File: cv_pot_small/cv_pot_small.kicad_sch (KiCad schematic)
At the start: 12 parts, among them J1 I/O connector, U1 HT7550-1, U2 LMV321IDBVR

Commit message: Updated components for JLCPCB PCBA
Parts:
- C1, C2: footprint Capacitor_SMD:C_0603_1608Metric -> Capacitor_SMD:C_0805_2012Metric; LCSC (none) -> C15850
- C3: footprint Capacitor_SMD:C_0603_1608Metric -> Capacitor_SMD:C_0402_1005Metric; LCSC (none) -> C307331
- D1: value LL4148 -> 1N4148W; footprint Diode_SMD:D_MiniMELF -> Diode_SMD:D_SOD-123; LCSC (none) -> C81598
- R1: value 5k -> 4.7k; footprint Resistor_SMD:R_0603_1608Metric -> Resistor_SMD:R_0402_1005Metric; LCSC (none) -> C25900
- U1: LCSC (none) -> C16106
- U2: LCSC (none) -> C7972
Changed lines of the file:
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@@
     (in_bom yes) (on_board yes) (fields_autoplaced)
     (property "Reference" "D1" (id 0) (at 92.71 43.5442 0))
-    (property "Value" "LL4148" (id 1) (at 92.71 46.0811 0))
-    (property "Footprint" "Diode_SMD:D_MiniMELF" (id 2) (at 92.71 48.26 90)
+    (property "Value" "1N4148W" (id 1) (at 92.71 46.0811 0))
+    (property "Footprint" "Diode_SMD:D_SOD-123" (id 2) (at 92.71 48.26 90)
       (effects (font (size 1.27 1.27)) hide)
     )
     (property "Datasheet" "~" (id 3) (at 92.71 48.26 90)
       (effects (font (size 1.27 1.27)) hide)
+    )
+    (property "LCSC" "C81598" (id 4) (at 92.71 48.26 0)
+      (effects (font (size 0 0)) hide)
     )
     (pin "1")
@@
       (effects (font (size 1.27 1.27)) (justify left))
     )
-    (property "Value" "5k" (id 1) (at 117.348 109.6522 0)
-      (effects (font (size 1.27 1.27)) (justify left))
-    )
-    (property "Footprint" "Resistor_SMD:R_0603_1608Metric" (id 2) (at 113.792 107.95 90)
+    (property "Value" "4.7k" (id 1) (at 117.348 109.6522 0)
+      (effects (font (size 1.27 1.27)) (justify left))
+    )
+    (property "Footprint" "Resistor_SMD:R_0402_1005Metric" (id 2) (at 113.792 107.95 90)
       (effects (font (size 1.27 1.27)) hide)
     )
@@
       (effects (font (size 1.27 1.27)) hide)
     )
+    (property "LCSC" "C25900" (id 4) (at 115.57 107.95 0)
+      (effects (font (size 1.524 1.524)) hide)
+    )
     (pin "1")
     (pin "2")
@@
       (effects (font (size 1.27 1.27)) (justify left))
     )
-    (property "Footprint" "Capacitor_SMD:C_0603_1608Metric" (id 2) (at 99.06 54.61 0)
+    (property "Footprint" "Capacitor_SMD:C_0805_2012Metric" (id 2) (at 99.06 54.61 0)
       (effects (font (size 1.27 1.27)) hide)
     )
     (property "Datasheet" "~" (id 3) (at 99.06 54.61 0)
       (effects (font (size 1.27 1.27)) hide)
+    )
+    (property "LCSC" "C15850" (id 4) (at 99.06 54.61 0)
+      (effects (font (size 1.524 1.524)) hide)
     )
     (pin "1")
@@
       (effects (font (size 1.27 1.27)) (justify left))
     )
-    (property "Footprint" "Capacitor_SMD:C_0603_1608Metric" (id 2) (at 120.65 54.61 0)
+    (property "Footprint" "Capacitor_SMD:C_0805_2012Metric" (id 2) (at 120.65 54.61 0)
       (effects (font (size 1.27 1.27)) hide)
     )
     (property "Datasheet" "~" (id 3) (at 120.65 54.61 0)
       (effects (font (size 1.27 1.27)) hide)
+    )
+    (property "LCSC" "C15850" (id 4) (at 120.65 54.61 0)
+      (effects (font (size 1.524 1.524)) hide)
     )
     (pin "1")
@@
     (property "Datasheet" "" (id 3) (at 123.19 68.58 0)
       (effects (font (size 1.27 1.27)) hide)
+    )
+    (property "LCSC" "C16106" (id 4) (at 110.49 48.26 0)
+      (effects (font (size 1.524 1.524)) hide)
     )
     (pin "1")
@@
       (effects (font (size 1.27 1.27)) (justify left))
     )
-    (property "Footprint" "Capacitor_SMD:C_0603_1608Metric" (id 2) (at 102.87 109.22 0)
+    (property "Footprint" "Capacitor_SMD:C_0402_1005Metric" (id 2) (at 102.87 109.22 0)
       (effects (font (size 1.27 1.27)) hide)
     )
     (property "Datasheet" "~" (id 3) (at 102.87 109.22 0)
       (effects (font (size 1.27 1.27)) hide)
+    )
+    (property "LCSC" "C307331" (id 4) (at 102.87 109.22 0)
+      (effects (font (size 1.524 1.524)) hide)
     )
     (pin "1")
@@
       (effects (font (size 1.27 1.27)) hide)
     )
+    (property "LCSC" "C7972" (id 4) (at 144.78 104.14 0)
+      (effects (font (size 1.524 1.524)) hide)
+    )
     (pin "2")
     (pin "5")
@@
     )
     (path "/86c1bc55-91df-4d16-85e2-6d6f7d6271c1"
-      (reference "C1") (unit 1) (value "10uF") (footprint "Capacitor_SMD:C_0603_1608Metric")
+      (reference "C1") (unit 1) (value "10uF") (footprint "Capacitor_SMD:C_0805_2012Metric")
     )
     (path "/a3049626-42e2-4901-9209-abf8037b2db1"
-      (reference "C2") (unit 1) (value "10uF") (footprint "Capacitor_SMD:C_0603_1608Metric")
+      (reference "C2") (unit 1) (value "10uF") (footprint "Capacitor_SMD:C_0805_2012Metric")
     )
     (path "/df012169-550a-4669-be77-71f4a184b60e"
-      (reference "C3") (unit 1) (value "100nF") (footprint "Capacitor_SMD:C_0603_1608Metric")
+      (reference "C3") (unit 1) (value "100nF") (footprint "Capacitor_SMD:C_0402_1005Metric")
     )
     (path "/205fc7e2-1cc5-48bb-8388-e8d2d06d6d0f"
-      (reference "D1") (unit 1) (value "LL4148") (footprint "Diode_SMD:D_MiniMELF")
+      (reference "D1") (unit 1) (value "1N4148W") (footprint "Diode_SMD:D_SOD-123")
     )
     (path "/bbeff794-ca6d-4e4a-ac80-c69c780af677"
@@
     )
     (path "/7b3b0a10-97e8-4760-9212-cec2185ba7eb"
-      (reference "R1") (unit 1) (value "5k") (footprint "Resistor_SMD:R_0603_1608Metric")
+      (reference "R1") (unit 1) (value "4.7k") (footprint "Resistor_SMD:R_0402_1005Metric")
     )
     (path "/9763309a-c9ed-492f-a4a9-0b6f407725b0"

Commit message: Added big CV pot
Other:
- company: Document Number: 2022002 -> Document Number: 2022004
- title: 5-way CV Module -> CV Pot Small
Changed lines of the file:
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@@
   (paper "A4")
   (title_block
-    (title "5-way CV Module")
+    (title "CV Pot Small")
     (date "2022-02-24")
     (rev "v3.0")
-    (company "Document Number: 2022002")
+    (company "Document Number: 2022004")
   )
   (junction (at 201.93 120.65) (diameter 0) (color 0 0 0 0)

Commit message: Switched to TLV6001UIDBVR Opamp
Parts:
- U2: value LMV321IDBVR -> TLV6001UIDBVR; LCSC C7972 -> (none)
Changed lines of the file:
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@@
     (in_bom yes) (on_board yes)
     (property "Reference" "U2" (id 0) (at 153.67 96.52 0))
-    (property "Value" "LMV321IDBVR" (id 1) (at 153.67 99.0569 0))
+    (property "Value" "TLV6001UIDBVR" (id 1) (at 153.67 99.0569 0))
     (property "Footprint" "Package_TO_SOT_SMD:SOT-23-5" (id 2) (at 142.24 109.22 0)
       (effects (font (size 1.27 1.27)) (justify left) hide)
@@
     (property "Datasheet" "" (id 3) (at 144.78 99.06 0)
       (effects (font (size 1.27 1.27)) hide)
-    )
-    (property "LCSC" "C7972" (id 4) (at 144.78 104.14 0)
-      (effects (font (size 1.524 1.524)) hide)
     )
     (pin "2")
@@
     )
     (path "/e69c64f9-717d-4a97-b3df-80325ec2fa63"
-      (reference "U2") (unit 1) (value "LMV321IDBVR") (footprint "Package_TO_SOT_SMD:SOT-23-5")
+      (reference "U2") (unit 1) (value "TLV6001UIDBVR") (footprint "Package_TO_SOT_SMD:SOT-23-5")
     )
   )

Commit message: Changed taper resistor value
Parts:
- R1: value 4.7k -> 47k; LCSC C25900 -> C25792
- RV1: value 25k -> 250k
- U1: JLCPCB_CORRECTION (none) -> 0;0;180
- U2: JLCPCB_CORRECTION (none) -> 0;0;180; LCSC (none) -> C544299
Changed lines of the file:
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@@
       (effects (font (size 1.27 1.27)) (justify left))
     )
-    (property "Value" "4.7k" (id 1) (at 117.348 109.6522 0)
+    (property "Value" "47k" (id 1) (at 117.348 109.6522 0)
       (effects (font (size 1.27 1.27)) (justify left))
     )
@@
       (effects (font (size 1.27 1.27)) hide)
     )
-    (property "LCSC" "C25900" (id 4) (at 115.57 107.95 0)
+    (property "LCSC" "C25792" (id 4) (at 115.57 107.95 0)
       (effects (font (size 1.524 1.524)) hide)
     )
@@
       (effects (font (size 1.27 1.27)) (justify right))
     )
-    (property "Value" "25k" (id 1) (at 87.1221 103.3022 0)
+    (property "Value" "250k" (id 1) (at 87.1221 103.3022 0)
       (effects (font (size 1.27 1.27)) (justify right))
     )
@@
       (effects (font (size 1.524 1.524)) hide)
     )
+    (property "JLCPCB_CORRECTION" "0;0;180" (id 5) (at 110.49 48.26 0)
+      (effects (font (size 1.27 1.27)) hide)
+    )
     (pin "1")
     (pin "2")
@@
       (effects (font (size 1.27 1.27)) hide)
     )
+    (property "LCSC" "C544299" (id 4) (at 144.78 104.14 0)
+      (effects (font (size 1.524 1.524)) hide)
+    )
+    (property "JLCPCB_CORRECTION" "0;0;180" (id 5) (at 144.78 104.14 0)
+      (effects (font (size 1.524 1.524)) hide)
+    )
     (pin "2")
     (pin "5")
@@
     )
     (path "/7b3b0a10-97e8-4760-9212-cec2185ba7eb"
-      (reference "R1") (unit 1) (value "4.7k") (footprint "Resistor_SMD:R_0402_1005Metric")
+      (reference "R1") (unit 1) (value "47k") (footprint "Resistor_SMD:R_0402_1005Metric")
     )
     (path "/9763309a-c9ed-492f-a4a9-0b6f407725b0"
-      (reference "RV1") (unit 1) (value "25k") (footprint "cycfi_library:bourns_pdb181")
+      (reference "RV1") (unit 1) (value "250k") (footprint "cycfi_library:bourns_pdb181")
     )
     (path "/b29e7a3c-8a61-4d5d-8478-053e45b60270"

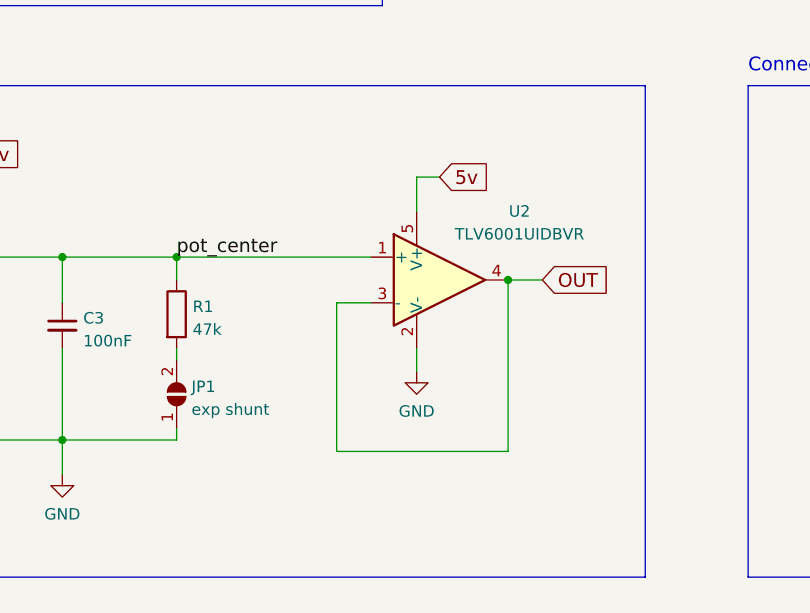
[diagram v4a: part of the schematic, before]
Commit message: Added 1k output resistor
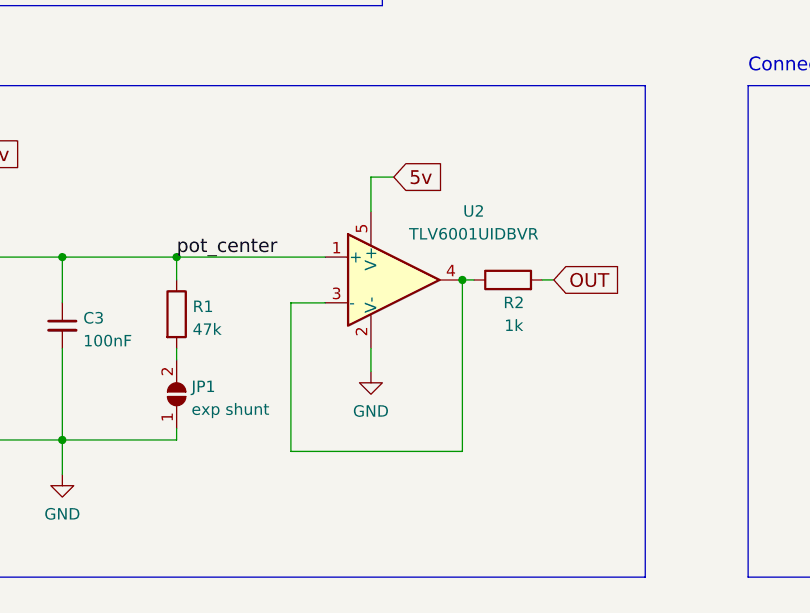
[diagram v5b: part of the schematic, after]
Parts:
- added R2: 1k, Resistor_SMD:R_0402_1005Metric, symbol Device:R
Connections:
- net OUT: now also R2.2; no longer U2.3 (-), U2.4
- new net: R2.1, U2.3 (-), U2.4
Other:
- moved on the sheet: U2
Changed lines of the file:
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@@
   (junction (at 99.06 48.26) (diameter 0) (color 0 0 0 0)
   )
-  (junction (at 152.4 104.14) (diameter 0) (color 0 0 0 0)
-  )
   (junction (at 120.65 59.69) (diameter 0) (color 0 0 0 0)
   )
+  (junction (at 147.32 104.14) (diameter 0) (color 0 0 0 0)
+  )
   (junction (at 102.87 101.6) (diameter 0) (color 0 0 0 0)
   )
@@
     (stroke (width 0) (type default) (color 0 0 0 0))
   )
-  (wire (pts (xy 133.35 123.19) (xy 152.4 123.19))
-    (stroke (width 0) (type default) (color 0 0 0 0))
-  )
-  (wire (pts (xy 152.4 104.14) (xy 152.4 123.19))
+  (wire (pts (xy 128.27 123.19) (xy 147.32 123.19))
+    (stroke (width 0) (type default) (color 0 0 0 0))
+  )
+  (wire (pts (xy 147.32 104.14) (xy 147.32 123.19))
     (stroke (width 0) (type default) (color 0 0 0 0))
   )
@@
     (stroke (width 0) (type default) (color 0 0 0 0))
   )
-  (wire (pts (xy 152.4 104.14) (xy 156.21 104.14))
-    (stroke (width 0) (type default) (color 0 0 0 0))
-  )
   (wire (pts (xy 120.65 59.69) (xy 124.46 59.69))
     (stroke (width 0) (type default) (color 0 0 0 0))
@@
     (stroke (width 0) (type default) (color 0 0 0 0))
   )
-  (wire (pts (xy 142.24 111.76) (xy 142.24 114.3))
+  (wire (pts (xy 137.16 111.76) (xy 137.16 114.3))
     (stroke (width 0) (type default) (color 0 0 0 0))
   )
@@
     (stroke (width 0) (type default) (color 0 0 0 0))
   )
-  (wire (pts (xy 142.24 92.71) (xy 144.78 92.71))
+  (wire (pts (xy 137.16 92.71) (xy 139.7 92.71))
     (stroke (width 0) (type default) (color 0 0 0 0))
   )
@@
     (stroke (width 0) (type default) (color 0 0 0 0))
   )
+  (wire (pts (xy 147.32 104.14) (xy 148.59 104.14))
+    (stroke (width 0) (type default) (color 0 0 0 0))
+  )
   (polyline (pts (xy 167.64 137.16) (xy 78.74 137.16))
     (stroke (width 0) (type default) (color 0 0 0 0))
@@
     (stroke (width 0) (type default) (color 0 0 0 0))
   )
-  (wire (pts (xy 133.35 106.68) (xy 133.35 123.19))
-    (stroke (width 0) (type default) (color 0 0 0 0))
-  )
-  (wire (pts (xy 137.16 106.68) (xy 133.35 106.68))
+  (wire (pts (xy 156.21 104.14) (xy 157.48 104.14))
+    (stroke (width 0) (type default) (color 0 0 0 0))
+  )
+  (wire (pts (xy 128.27 106.68) (xy 128.27 123.19))
+    (stroke (width 0) (type default) (color 0 0 0 0))
+  )
+  (wire (pts (xy 132.08 106.68) (xy 128.27 106.68))
     (stroke (width 0) (type default) (color 0 0 0 0))
   )
@@
     (stroke (width 0) (type default) (color 0 0 0 0))
   )
-  (wire (pts (xy 142.24 96.52) (xy 142.24 92.71))
+  (wire (pts (xy 137.16 96.52) (xy 137.16 92.71))
     (stroke (width 0) (type default) (color 0 0 0 0))
   )
@@
     (stroke (width 0) (type default) (color 0 0 0 0))
   )
-  (wire (pts (xy 115.57 101.6) (xy 137.16 101.6))
+  (wire (pts (xy 115.57 101.6) (xy 132.08 101.6))
     (stroke (width 0) (type default) (color 0 0 0 0))
   )
@@
     )
   )
-  (global_label "5v" (shape input) (at 144.78 92.71 0) (fields_autoplaced)
+  (global_label "5v" (shape input) (at 139.7 92.71 0) (fields_autoplaced)
     (effects (font (size 1.524 1.524)) (justify left))
-    (property "Intersheet References" "${INTERSHEET_REFS}" (id 0) (at 150.1815 92.6148 0)
+    (property "Intersheet References" "${INTERSHEET_REFS}" (id 0) (at 145.1015 92.6148 0)
       (effects (font (size 1.524 1.524)) (justify left) hide)
     )
@@
     )
   )
-  (global_label "OUT" (shape input) (at 156.21 104.14 0) (fields_autoplaced)
+  (global_label "OUT" (shape input) (at 157.48 104.14 0) (fields_autoplaced)
     (effects (font (size 1.524 1.524)) (justify left))
-    (property "Intersheet References" "${INTERSHEET_REFS}" (id 0) (at 163.3532 104.0448 0)
+    (property "Intersheet References" "${INTERSHEET_REFS}" (id 0) (at 164.6232 104.0448 0)
       (effects (font (size 1.524 1.524)) (justify left) hide)
     )
@@
     (pin "1")
   )
-  (symbol (lib_id "power:GND") (at 142.24 114.3 0) (unit 1)
-    (in_bom yes) (on_board yes) (fields_autoplaced)
-    (property "Reference" "#PWR05" (id 0) (at 142.24 120.65 0)
-      (effects (font (size 1.27 1.27)) hide)
-    )
-    (property "Value" "GND" (id 1) (at 142.24 118.7434 0))
-    (property "Footprint" "" (id 2) (at 142.24 114.3 0)
-      (effects (font (size 1.27 1.27)) hide)
-    )
-    (property "Datasheet" "" (id 3) (at 142.24 114.3 0)
+  (symbol (lib_id "power:GND") (at 137.16 114.3 0) (unit 1)
+    (in_bom yes) (on_board yes) (fields_autoplaced)
+    (property "Reference" "#PWR05" (id 0) (at 137.16 120.65 0)
+      (effects (font (size 1.27 1.27)) hide)
+    )
+    (property "Value" "GND" (id 1) (at 137.16 118.7434 0))
+    (property "Footprint" "" (id 2) (at 137.16 114.3 0)
+      (effects (font (size 1.27 1.27)) hide)
+    )
+    (property "Datasheet" "" (id 3) (at 137.16 114.3 0)
       (effects (font (size 1.27 1.27)) hide)
     )
@@
     (pin "2")
   )
-  (symbol (lib_id "cycfi_library:opamp_dbv2") (at 144.78 104.14 0) (unit 1)
+  (symbol (lib_id "Device:R") (at 152.4 104.14 90) (unit 1)
     (in_bom yes) (on_board yes)
-    (property "Reference" "U2" (id 0) (at 153.67 96.52 0))
-    (property "Value" "TLV6001UIDBVR" (id 1) (at 153.67 99.0569 0))
-    (property "Footprint" "Package_TO_SOT_SMD:SOT-23-5" (id 2) (at 142.24 109.22 0)
+    (property "Reference" "R2" (id 0) (at 153.035 106.6831 90))
+    (property "Value" "1k" (id 1) (at 153.035 109.22 90))
+    (property "Footprint" "Resistor_SMD:R_0402_1005Metric" (id 2) (at 152.4 105.918 90)
+      (effects (font (size 1.27 1.27)) hide)
+    )
+    (property "Datasheet" "~" (id 3) (at 152.4 104.14 0)
+      (effects (font (size 1.27 1.27)) hide)
+    )
+    (property "LCSC" "C11702" (id 4) (at 152.4 104.14 0)
+      (effects (font (size 1.524 1.524)) hide)
+    )
+    (pin "1")
+    (pin "2")
+  )
+  (symbol (lib_id "cycfi_library:opamp_dbv2") (at 139.7 104.14 0) (unit 1)
+    (in_bom yes) (on_board yes)
+    (property "Reference" "U2" (id 0) (at 148.59 96.52 0))
+    (property "Value" "TLV6001UIDBVR" (id 1) (at 148.59 99.0569 0))
+    (property "Footprint" "Package_TO_SOT_SMD:SOT-23-5" (id 2) (at 137.16 109.22 0)
       (effects (font (size 1.27 1.27)) (justify left) hide)
     )
-    (property "Datasheet" "" (id 3) (at 144.78 99.06 0)
-      (effects (font (size 1.27 1.27)) hide)
-    )
-    (property "LCSC" "C544299" (id 4) (at 144.78 104.14 0)
-      (effects (font (size 1.524 1.524)) hide)
-    )
-    (property "JLCPCB_CORRECTION" "0;0;180" (id 5) (at 144.78 104.14 0)
+    (property "Datasheet" "" (id 3) (at 139.7 99.06 0)
+      (effects (font (size 1.27 1.27)) hide)
+    )
+    (property "LCSC" "C544299" (id 4) (at 139.7 104.14 0)
+      (effects (font (size 1.524 1.524)) hide)
+    )
+    (property "JLCPCB_CORRECTION" "0;0;180" (id 5) (at 139.7 104.14 0)
       (effects (font (size 1.524 1.524)) hide)
     )
@@
       (reference "R1") (unit 1) (value "47k") (footprint "Resistor_SMD:R_0402_1005Metric")
     )
+    (path "/e118eae4-09e9-403d-850d-5d7c65836c22"
+      (reference "R2") (unit 1) (value "1k") (footprint "Resistor_SMD:R_0402_1005Metric")
+    )
     (path "/9763309a-c9ed-492f-a4a9-0b6f407725b0"
